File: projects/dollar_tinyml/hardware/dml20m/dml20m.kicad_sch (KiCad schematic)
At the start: 25 parts, among them J2 USB_A, J4 Header 2.54mm, SW1 SW_Push, U1 PY32F003F16P6TU, U2 LP4054HB5F, U3 BM7161, U4 XC6206PxxxMR, U6 LIS2DH12

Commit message: dollarml: Some tweaks
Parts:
- removed J4: Header 2.54mm, Connector_PinHeader_2.54mm:PinHeader_1x14_P2.54mm_Vertical, symbol Connector_Generic:Conn_01x14
- added J1, J4: Header 2.54mm, Connector_JST:JST_SH_SM04B-SRSS-TB_1x04-1MP_P1.00mm_Horizontal, symbol Connector_Generic:Conn_01x04
- added J3: Conn_ARM_SWD_TagConnect_TC2030-NL, Connector:Tag-Connect_TC2030-IDC-NL_2x03_P1.27mm_Vertical, symbol Connector:Conn_ARM_SWD_TagConnect_TC2030-NL
- BT1: footprint Connector_PinHeader_2.54mm:PinHeader_1x02_P2.54mm_Vertical -> dml20m:Battery_CR1220-Horizontal
- D3: footprint (none) -> LED_SMD:LED_RGB_5050-6; symbol Device:LED_RGB -> dml20m:LED_RGB_5050_6p
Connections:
- net BOOT0: now also J4.1 (Pin_1)
- net GND: now also J1.4 (Pin_4), J3.5 (GND)
- net LED_BLUE_P: now also D3.3 (BK)
- net LED_GREEN_P: now also D3.1 (RK)
- net LED_RED_P: now also D3.2 (GK)
- net RESET: now also J3.3 (~{RESET})
- net SCL: now also J1.2 (Pin_2)
- net SDA: now also J1.3 (Pin_3)
- net SWCLK: now also J3.4 (SWCLK)
- net SWDIO: now also J3.2 (SWDIO)
- net VDD: now also J1.1 (Pin_1), J3.1 (VCC)
- net at R2.1: now also D3.4 (BA)
- net at R13.1: now also D3.5 (GA)
- net at R3.1: now also D3.6 (RA)
- net AUDIO_HIGH: no longer names the net of U1.20 (PA1)
- net AUDIO_LOW: no longer names the net of U1.19 (PA0)
- net LED_WHITE_N: no longer names the net of U1.14 (PB7)
- net MIC_POWER_CTRL: no longer names the net of U1.8 (PA12)
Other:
- note added: "FIXME: update pinout"
- note added: "Headers"
- note added: "TODO: add some GPIO"
- note removed: "FIXME: add battery connector"
- note removed: "Header"
- note removed: "dd"
- moved on the sheet: D3, R13, R2, R3, R5

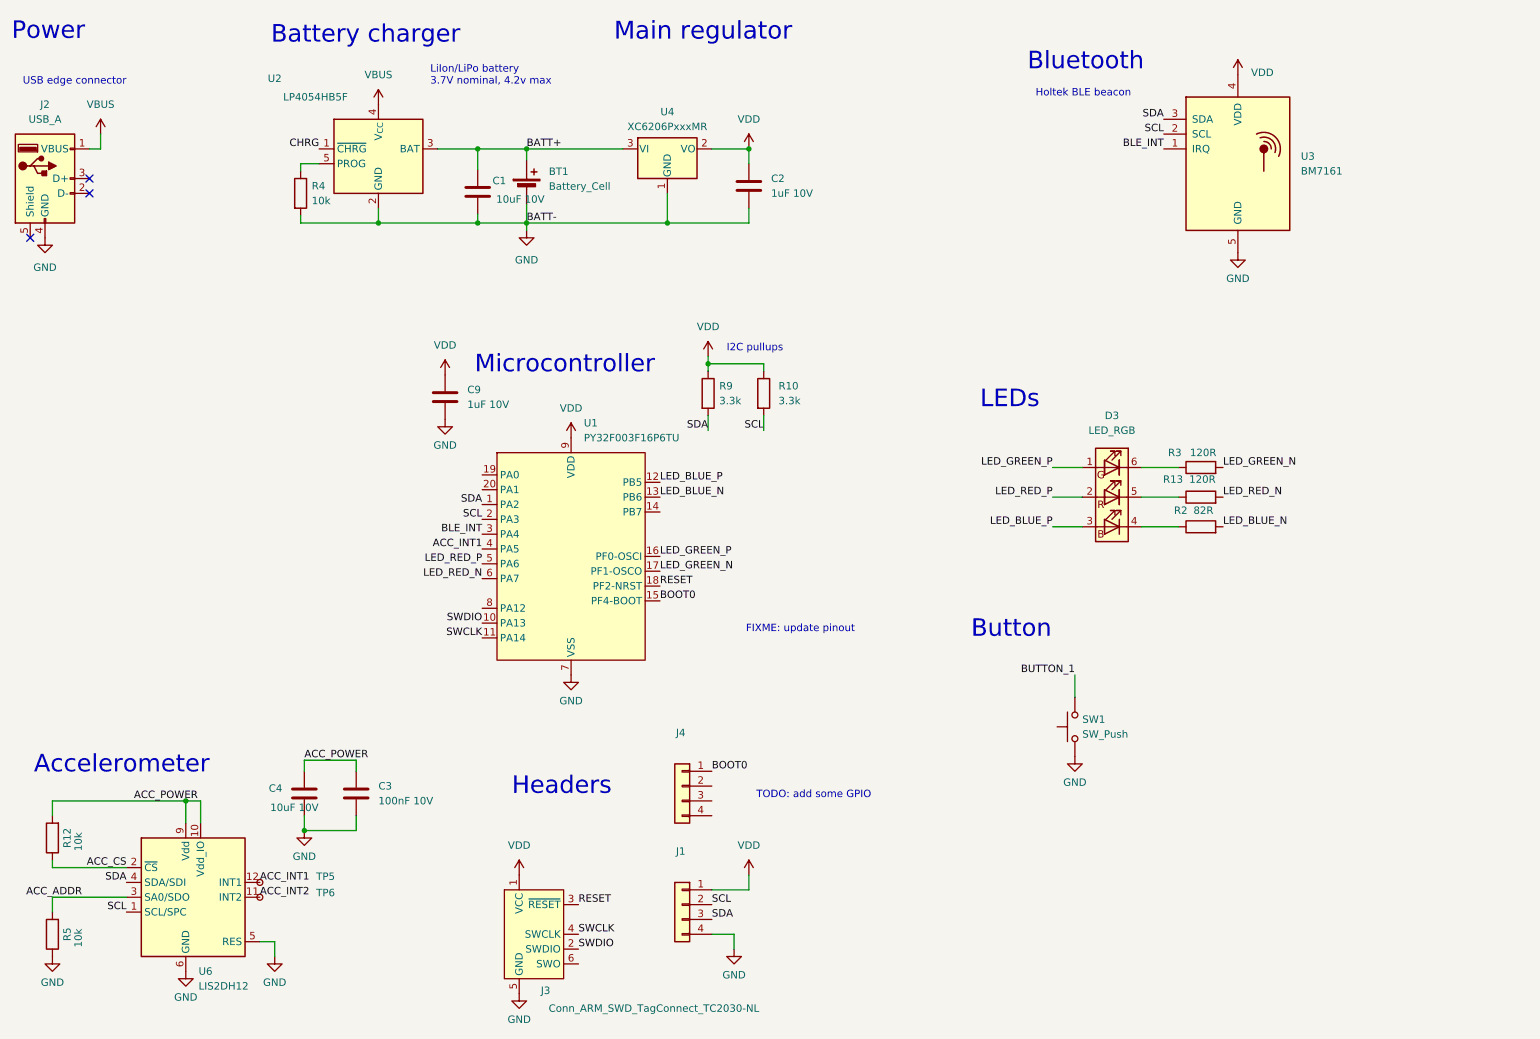
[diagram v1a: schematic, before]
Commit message: dollarml: Almost everything routed
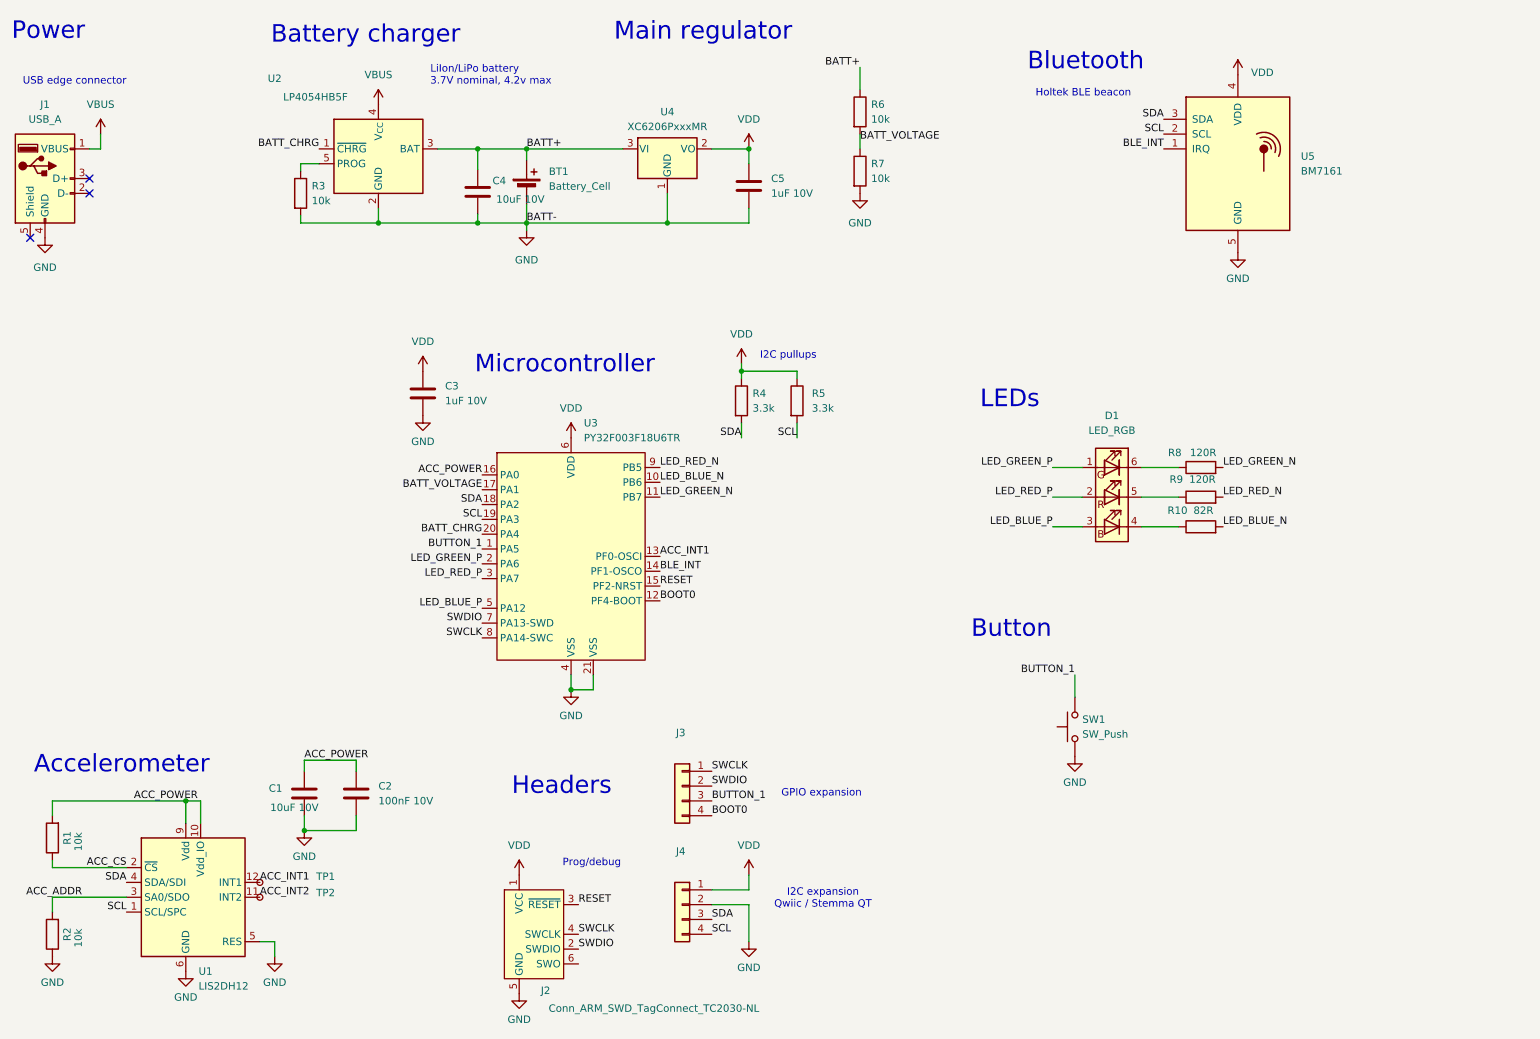
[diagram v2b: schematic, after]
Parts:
- added R6, R7: 10k, Resistor_SMD:R_0603_1608Metric, symbol Device:R
- U3: renamed from U1; value PY32F003F16P6TU -> PY32F003F18U6TR; symbol dml10:PY32F003F1xP -> dml20m:PY32F003F1xU
- renumbered C4 to C1, C3 to C2, C9 to C3, C1 to C4, C2 to C5, D3 to D1, J2 to J1, J3 to J2, J4 to J3, J1 to J4, R12 to R1, R2 to R10, R5 to R2, R4 to R3, R9 to R4, R10 to R5, R3 to R8, R13 to R9, TP5 to TP1, TP6 to TP2, U6 to U1, U3 to U5
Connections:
- net CHRG is gone; now on net BATT_CHRG: U2.1 (~{CHRG})
- net ACC_INT1: now also U3.13 (PF0-OSCI); no longer U3.4 (PA5)
- net ACC_POWER: now also U3.16 (PA0)
- net BATT+: now also R6.1
- net BLE_INT: now also U3.14 (PF1-OSCO); no longer U3.3 (PA4)
- net BOOT0: now also J3.4 (Pin_4), U3.12 (PF4-BOOT); no longer J3.1 (Pin_1), U3.15 (PF4-BOOT)
- net BUTTON_1: now also J3.3 (Pin_3), U3.1 (PA5)
- net GND: now also J4.2 (Pin_2), U3.21 (VSS), U3.4 (VSS), R7.2; no longer J4.4 (Pin_4), U3.7 (VSS)
- net LED_BLUE_N: now also U3.10 (PB6); no longer U3.13 (PB6)
- net LED_BLUE_P: now also U3.5 (PA12); no longer U3.12 (PB5)
- net LED_GREEN_N: now also U3.11 (PB7); no longer U3.17 (PF1-OSCO)
- net LED_GREEN_P: now also U3.2 (PA6); no longer U3.16 (PF0-OSCI)
- net LED_RED_N: now also U3.9 (PB5); no longer U3.6 (PA7)
- net LED_RED_P: now also U3.3 (PA7); no longer U3.5 (PA6)
- net RESET: now also U3.15 (PF2-NRST); no longer U3.18 (PF2-NRST)
- net SCL: now also J4.4 (Pin_4), U3.19 (PA3); no longer J4.2 (Pin_2), U3.2 (PA3)
- net SDA: now also U3.18 (PA2); no longer U3.1 (PA2)
- net SWCLK: now also J3.1 (Pin_1), U3.8 (PA14-SWC); no longer U3.11 (PA14)
- net SWDIO: now also J3.2 (Pin_2), U3.7 (PA13-SWD); no longer U3.10 (PA13)
- net VDD: now also U3.6 (VDD); no longer U3.9 (VDD)
- net BATT_CHRG: now reaches U3.20 (PA4)
- new net BATT_VOLTAGE: R6.2, R7.1, U3.17 (PA1)
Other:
- note added: "GPIO expansion"
- note added: "I2C expansion Qwiic / Stemma QT"
- note added: "Prog/debug"
- note removed: "FIXME: update pinout"
- note removed: "TODO: add some GPIO"
- moved on the sheet: C3, R4, R5

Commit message: dollarml: Split I2C to BLE, add buzzer
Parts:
- removed TP1: TP_PCB, TestPoint:TestPoint_Pad_D1.0mm, symbol Connector:TestPoint_Small
- added BZ1: Buzzer, Jumper:SolderJumper-2_P1.3mm_Open_Pad1.0x1.5mm, symbol Device:Buzzer
- added D2: 1N4001, Diode_SMD:D_SOD-123F, symbol Device:D_Small_Filled
- added JP1: SolderJumper_3_Bridged12, Jumper:SolderJumper-3_P1.3mm_Bridged12_RoundedPad1.0x1.5mm, symbol Jumper:SolderJumper_3_Bridged12
- added Q1: BC547B, Package_TO_SOT_SMD:SOT-23, symbol Device:Q_NPN_BCE
- added R11: 100R, Resistor_SMD:R_0603_1608Metric, symbol Device:R
- added R12: 33R, Resistor_SMD:R_0603_1608Metric, symbol Device:R
- added R13, R14: 3.3k, Resistor_SMD:R_0603_1608Metric, symbol Device:R
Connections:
- net ACC_INT1: now also JP1.3 (B); no longer U3.13 (PF0-OSCI)
- net BLE_INT: now also U3.13 (PF0-OSCI); no longer U3.14 (PF1-OSCO)
- net GND: now also R10.2, R9.2, Q1.3 (E)
- net LED_GREEN_N: now also U3.9 (PB5); no longer U3.11 (PB7)
- net SCL: no longer U5.2 (SCL)
- net SDA: no longer U5.3 (SDA)
- net VDD: now also R12.2, R13.1, R14.1
- net LED_BLUE_N renamed BLE_SCL
- net BLE_SCL: now also U5.2 (SCL), R14.2; no longer R10.2
- removed net LED_RED_N: R9.2, U3.9 (PB5)
- new net: Q1.1 (B), R11.2
- new net: BZ1.2 (-), D2.2 (A), Q1.2 (C)
- new net: BZ1.1 (+), D2.1 (K), R12.1
- new net ACC_INT/BUZZER: JP1.2 (C), U3.14 (PF1-OSCO)
- new net BLE_SDA: R13.2, U3.11 (PB7), U5.3 (SDA)
- new net BUZZER: JP1.1 (A), R11.1
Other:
- note added: "BC7161 is non-standard I2C, and should be alone on bus"
- note added: "Buzzer"
- note added: "FIXME: verify microcontroller and accelerometer pinout"
- note added: "FIXME: verify transistor and buzzer pinout"
- note added: "GPIO expansion SWCLK/SWDIO is UART1 RX/TX"
- note added: "Min 16 ohm"
- note removed: "GPIO expansion"
- moved on the sheet: D1, R10, R8, R9, U5

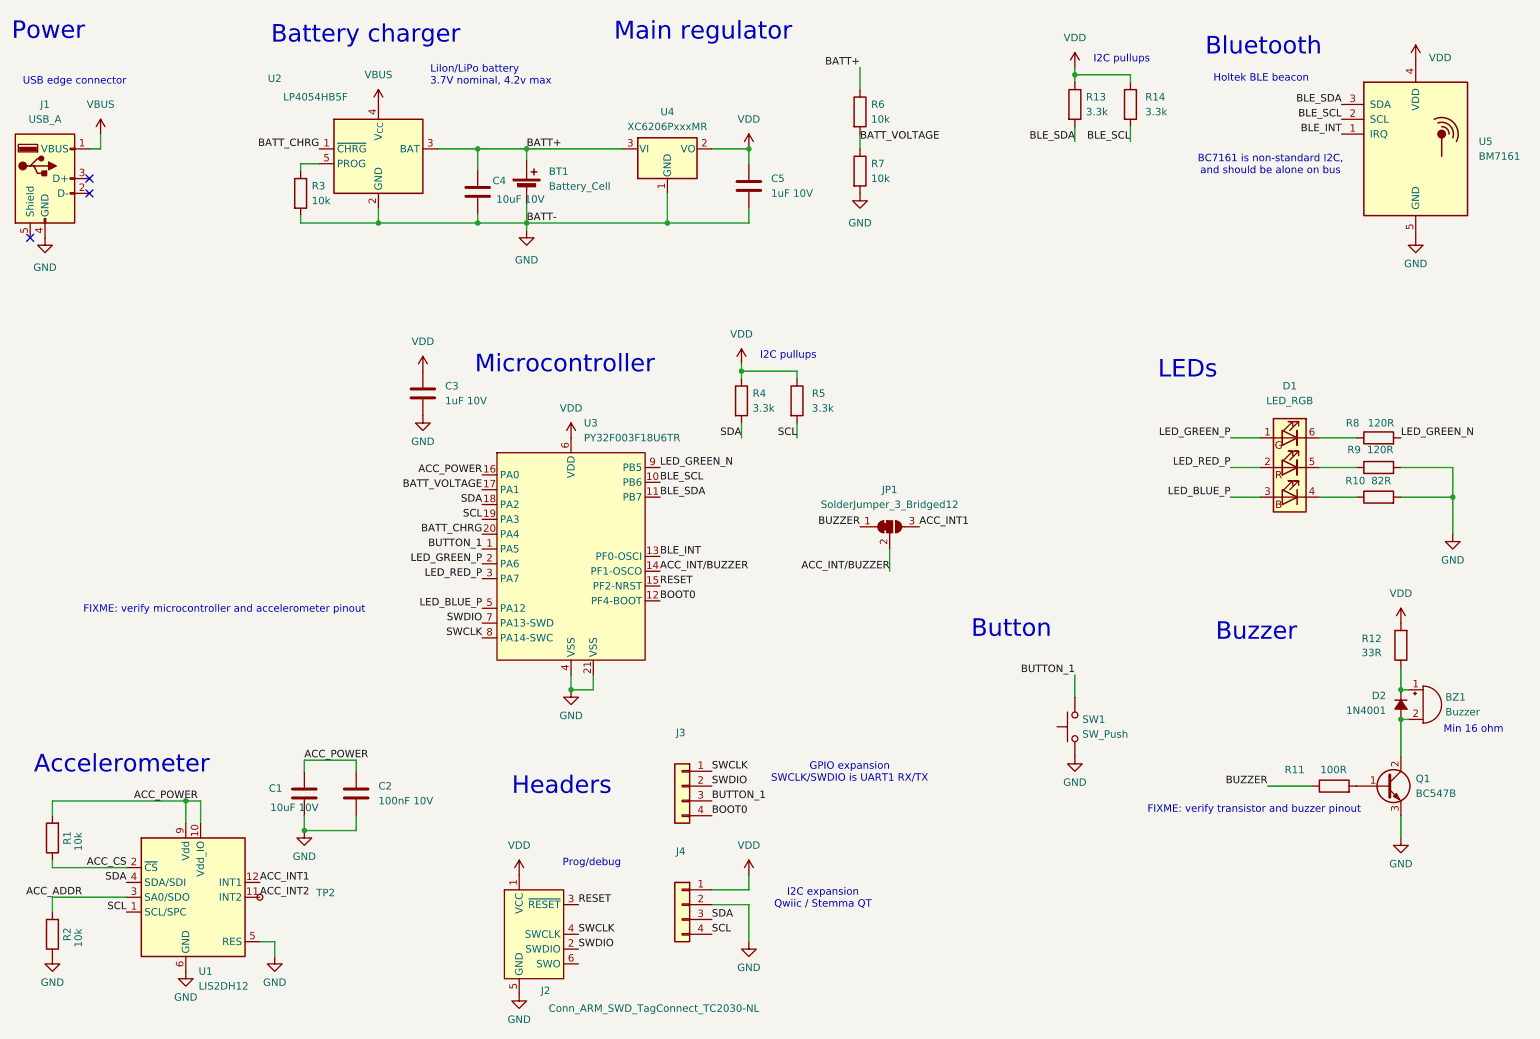
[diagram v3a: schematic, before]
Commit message: dollarml: Improve groundplane, remove via-in-pad
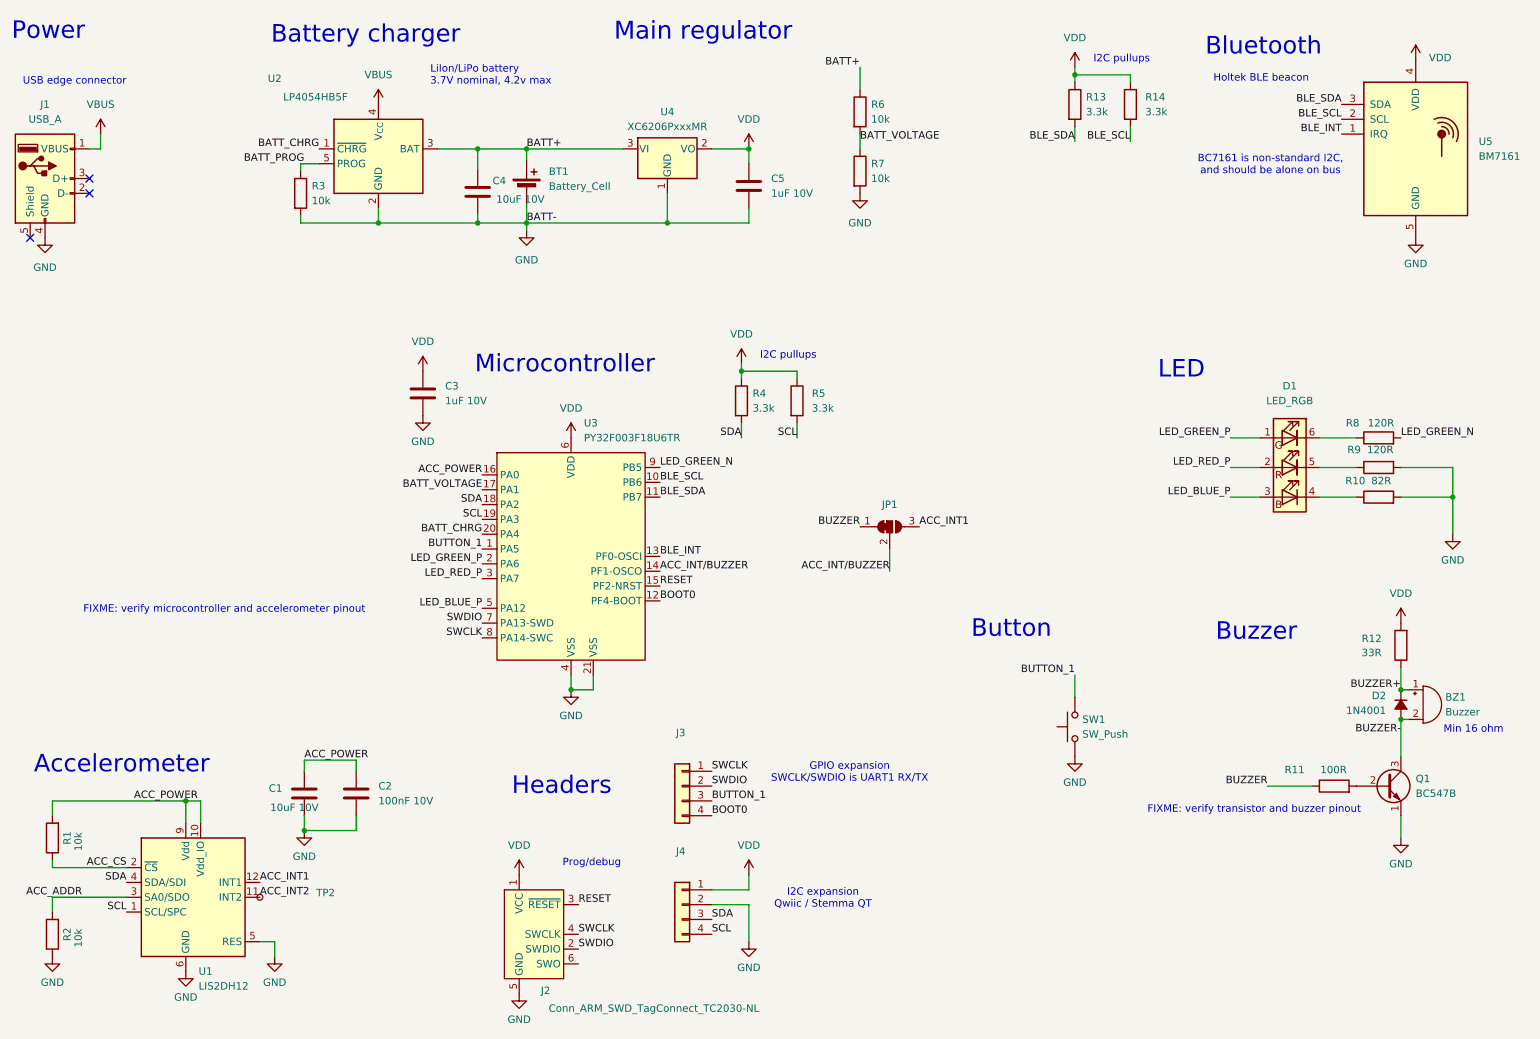
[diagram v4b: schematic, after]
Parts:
- Q1: symbol Device:Q_NPN_BCE -> Device:Q_NPN_EBC
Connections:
- net GND: now also Q1.1 (E); no longer Q1.3 (E)
- net at R11.2: now also Q1.2 (B); no longer Q1.1 (B)
- net BUZZER-: now reaches BZ1.2 (-), D2.2 (A)
- net BUZZER-: now also Q1.3 (C); no longer Q1.2 (C)
- net BUZZER+: now reaches BZ1.1 (+), D2.1 (K), R12.1
- net BATT_PROG: now reaches R3.1, U2.5 (PROG)
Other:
- note added: "LED"
- note removed: "LEDs"
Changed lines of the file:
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@@
 		)
 	)
-	(text "LEDs"
+	(text "LED"
 		(exclude_from_sim no)
 		(at 217.424 77.724 0)
@@
 		)
 	)
+	(label "BUZZER+"
+		(at 259.08 130.81 180)
+		(fields_autoplaced yes)
+		(effects
+			(font
+				(size 1.27 1.27)
+			)
+			(justify right bottom)
+		)
+	)
 	(label "BATT+"
 		(at 109.22 38.1 0)
@@
 		)
 	)
+	(label "BATT_PROG"
+		(at 71.12 40.64 180)
+		(fields_autoplaced yes)
+		(effects
+			(font
+				(size 1.27 1.27)
+			)
+			(justify right bottom)
+		)
+	)
 	(label "SCL"
 		(at 101.6 101.6 180)
@@
 	(label "SCL"
 		(at 40.64 168.91 180)
+		(fields_autoplaced yes)
+		(effects
+			(font
+				(size 1.27 1.27)
+			)
+			(justify right bottom)
+		)
+	)
+	(label "BUZZER-"
+		(at 259.08 138.43 180)
 		(fields_autoplaced yes)
 		(effects
@@
 	)
 	(symbol
-		(lib_id "Device:Q_NPN_BCE")
+		(lib_id "Device:Q_NPN_EBC")
 		(at 256.54 147.32 0)
 		(unit 1)
@@
 			)
 		)
-		(property "Description" "NPN transistor, base/collector/emitter"
+		(property "Description" "NPN transistor, emitter/base/collector"
 			(at 256.54 147.32 0)
 			(effects
@@
 		(fields_autoplaced yes)
 		(property "Reference" "JP1"
-			(at 171.45 96.52 0)
+			(at 171.45 99.06 0)
 			(effects
 				(font
@@
 					(size 1.27 1.27)
 				)
-			)
-		)
+				(hide yes)
+			)
+		)
